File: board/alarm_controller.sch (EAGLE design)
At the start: 150 parts, among them IC3 AT24C, X1 RJ45-8L21-S, X2 RJ45-8L21-S

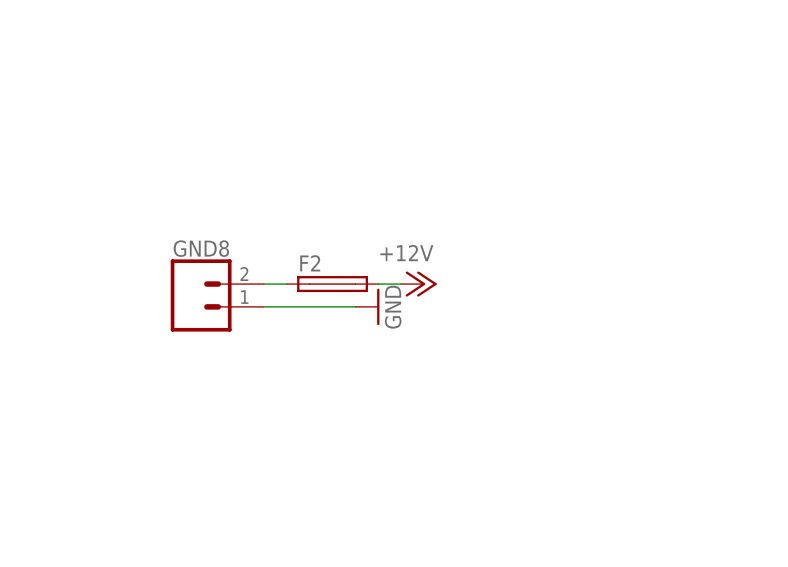
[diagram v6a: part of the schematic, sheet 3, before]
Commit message: swap pwr input for correct orientation
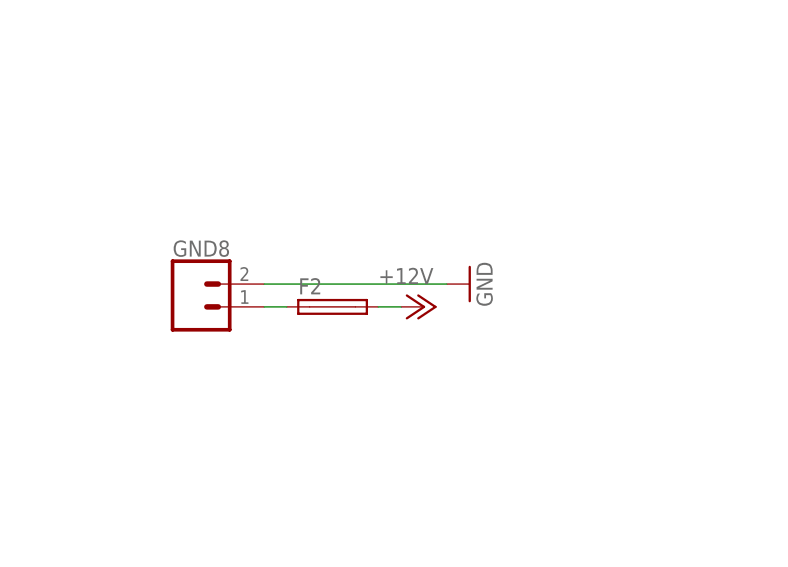
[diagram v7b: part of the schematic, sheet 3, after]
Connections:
- net GND: now also GND8.2; no longer GND8.1
- net PRE_FUSE_12V: now also GND8.1; no longer GND8.2
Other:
- moved on the sheet: F2
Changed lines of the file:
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@@
 <grid distance="0.1" unitdist="inch" unit="inch" style="lines" multiple="1" display="no" altdistance="0.01" altunitdist="inch" altunit="inch"/>
 <layers>
-<layer number="1" name="Top" color="4" fill="1" visible="yes" active="no"/>
-<layer number="2" name="Route2" color="1" fill="3" visible="yes" active="no"/>
-<layer number="3" name="Route3" color="4" fill="3" visible="yes" active="no"/>
-<layer number="4" name="Route4" color="1" fill="4" visible="yes" active="no"/>
-<layer number="5" name="Route5" color="4" fill="4" visible="yes" active="no"/>
-<layer number="6" name="Route6" color="1" fill="8" visible="yes" active="no"/>
-<layer number="7" name="Route7" color="4" fill="8" visible="yes" active="no"/>
-<layer number="8" name="Route8" color="1" fill="2" visible="yes" active="no"/>
-<layer number="9" name="Route9" color="4" fill="2" visible="yes" active="no"/>
-<layer number="10" name="Route10" color="1" fill="7" visible="yes" active="no"/>
-<layer number="11" name="Route11" color="4" fill="7" visible="yes" active="no"/>
-<layer number="12" name="Route12" color="1" fill="5" visible="yes" active="no"/>
-<layer number="13" name="Route13" color="4" fill="5" visible="yes" active="no"/>
-<layer number="14" name="Route14" color="1" fill="6" visible="yes" active="no"/>
-<layer number="15" name="Route15" color="4" fill="6" visible="yes" active="no"/>
-<layer number="16" name="Bottom" color="1" fill="1" visible="yes" active="no"/>
-<layer number="17" name="Pads" color="2" fill="1" visible="yes" active="no"/>
-<layer number="18" name="Vias" color="2" fill="1" visible="yes" active="no"/>
-<layer number="19" name="Unrouted" color="6" fill="1" visible="yes" active="no"/>
-<layer number="20" name="Dimension" color="15" fill="1" visible="yes" active="no"/>
-<layer number="21" name="tPlace" color="7" fill="1" visible="yes" active="no"/>
-<layer number="22" name="bPlace" color="7" fill="1" visible="yes" active="no"/>
-<layer number="23" name="tOrigins" color="15" fill="1" visible="yes" active="no"/>
-<layer number="24" name="bOrigins" color="15" fill="1" visible="yes" active="no"/>
-<layer number="25" name="tNames" color="7" fill="1" visible="yes" active="no"/>
-<layer number="26" name="bNames" color="7" fill="1" visible="yes" active="no"/>
-<layer number="27" name="tValues" color="7" fill="1" visible="yes" active="no"/>
-<layer number="28" name="bValues" color="7" fill="1" visible="yes" active="no"/>
+<layer number="1" name="Top" color="4" fill="1" visible="no" active="no"/>
+<layer number="2" name="Route2" color="1" fill="3" visible="no" active="no"/>
+<layer number="3" name="Route3" color="4" fill="3" visible="no" active="no"/>
+<layer number="4" name="Route4" color="1" fill="4" visible="no" active="no"/>
+<layer number="5" name="Route5" color="4" fill="4" visible="no" active="no"/>
+<layer number="6" name="Route6" color="1" fill="8" visible="no" active="no"/>
+<layer number="7" name="Route7" color="4" fill="8" visible="no" active="no"/>
+<layer number="8" name="Route8" color="1" fill="2" visible="no" active="no"/>
+<layer number="9" name="Route9" color="4" fill="2" visible="no" active="no"/>
+<layer number="10" name="Route10" color="1" fill="7" visible="no" active="no"/>
+<layer number="11" name="Route11" color="4" fill="7" visible="no" active="no"/>
+<layer number="12" name="Route12" color="1" fill="5" visible="no" active="no"/>
+<layer number="13" name="Route13" color="4" fill="5" visible="no" active="no"/>
+<layer number="14" name="Route14" color="1" fill="6" visible="no" active="no"/>
+<layer number="15" name="Route15" color="4" fill="6" visible="no" active="no"/>
+<layer number="16" name="Bottom" color="1" fill="1" visible="no" active="no"/>
+<layer number="17" name="Pads" color="2" fill="1" visible="no" active="no"/>
+<layer number="18" name="Vias" color="2" fill="1" visible="no" active="no"/>
+<layer number="19" name="Unrouted" color="6" fill="1" visible="no" active="no"/>
+<layer number="20" name="Dimension" color="15" fill="1" visible="no" active="no"/>
+<layer number="21" name="tPlace" color="7" fill="1" visible="no" active="no"/>
+<layer number="22" name="bPlace" color="7" fill="1" visible="no" active="no"/>
+<layer number="23" name="tOrigins" color="15" fill="1" visible="no" active="no"/>
+<layer number="24" name="bOrigins" color="15" fill="1" visible="no" active="no"/>
+<layer number="25" name="tNames" color="7" fill="1" visible="no" active="no"/>
+<layer number="26" name="bNames" color="7" fill="1" visible="no" active="no"/>
+<layer number="27" name="tValues" color="7" fill="1" visible="no" active="no"/>
+<layer number="28" name="bValues" color="7" fill="1" visible="no" active="no"/>
 <layer number="29" name="tStop" color="7" fill="3" visible="no" active="no"/>
 <layer number="30" name="bStop" color="7" fill="6" visible="no" active="no"/>
@@
 <layer number="35" name="tGlue" color="7" fill="4" visible="no" active="no"/>
 <layer number="36" name="bGlue" color="7" fill="5" visible="no" active="no"/>
-<layer number="37" name="tTest" color="7" fill="1" visible="yes" active="no"/>
-<layer number="38" name="bTest" color="7" fill="1" visible="yes" active="no"/>
+<layer number="37" name="tTest" color="7" fill="1" visible="no" active="no"/>
+<layer number="38" name="bTest" color="7" fill="1" visible="no" active="no"/>
 <layer number="39" name="tKeepout" color="4" fill="11" visible="no" active="no"/>
 <layer number="40" name="bKeepout" color="1" fill="11" visible="no" active="no"/>
@@
 <layer number="44" name="Drills" color="7" fill="1" visible="no" active="no"/>
 <layer number="45" name="Holes" color="7" fill="1" visible="no" active="no"/>
-<layer number="46" name="Milling" color="3" fill="1" visible="yes" active="no"/>
-<layer number="47" name="Measures" color="7" fill="1" visible="yes" active="no"/>
-<layer number="48" name="Document" color="7" fill="1" visible="yes" active="no"/>
-<layer number="49" name="Reference" color="7" fill="1" visible="yes" active="no"/>
-<layer number="50" name="dxf" color="7" fill="1" visible="yes" active="no"/>
-<layer number="51" name="tDocu" color="7" fill="1" visible="yes" active="no"/>
-<layer number="52" name="bDocu" color="7" fill="1" visible="yes" active="no"/>
-<layer number="53" name="tGND_GNDA" color="7" fill="9" visible="yes" active="no"/>
-<layer number="54" name="bGND_GNDA" color="1" fill="9" visible="yes" active="no"/>
-<layer number="56" name="wert" color="7" fill="1" visible="yes" active="no"/>
-<layer number="57" name="tCAD" color="7" fill="1" visible="yes" active="no"/>
-<layer number="59" name="tCarbon" color="7" fill="1" visible="yes" active="no"/>
-<layer number="60" name="bCarbon" color="7" fill="1" visible="yes" active="no"/>
+<layer number="46" name="Milling" color="3" fill="1" visible="no" active="no"/>
+<layer number="47" name="Measures" color="7" fill="1" visible="no" active="no"/>
+<layer number="48" name="Document" color="7" fill="1" visible="no" active="no"/>
+<layer number="49" name="Reference" color="7" fill="1" visible="no" active="no"/>
+<layer number="50" name="dxf" color="7" fill="1" visible="no" active="no"/>
+<layer number="51" name="tDocu" color="7" fill="1" visible="no" active="no"/>
+<layer number="52" name="bDocu" color="7" fill="1" visible="no" active="no"/>
+<layer number="53" name="tGND_GNDA" color="7" fill="9" visible="no" active="no"/>
+<layer number="54" name="bGND_GNDA" color="1" fill="9" visible="no" active="no"/>
+<layer number="56" name="wert" color="7" fill="1" visible="no" active="no"/>
+<layer number="57" name="tCAD" color="7" fill="1" visible="no" active="no"/>
+<layer number="59" name="tCarbon" color="7" fill="1" visible="no" active="no"/>
+<layer number="60" name="bCarbon" color="7" fill="1" visible="no" active="no"/>
 <layer number="90" name="Modules" color="5" fill="1" visible="yes" active="yes"/>
 <layer number="91" name="Nets" color="2" fill="1" visible="yes" active="yes"/>
@@
 <instance part="R62" gate="G$1" x="-81.28" y="35.56" rot="R180"/>
 <instance part="GND8" gate="G$1" x="-127" y="99.06"/>
-<instance part="F2" gate="1" x="-111.76" y="101.6"/>
-<instance part="P+8" gate="1" x="-101.6" y="101.6" rot="R270"/>
-<instance part="GND89" gate="1" x="-106.68" y="99.06" rot="R90"/>
+<instance part="F2" gate="1" x="-111.76" y="99.06"/>
+<instance part="P+8" gate="1" x="-101.6" y="99.06" rot="R270"/>
+<instance part="GND89" gate="1" x="-96.52" y="101.6" rot="R90"/>
 <instance part="12V2" gate="G$1" x="-43.18" y="35.56" rot="R180"/>
 <instance part="ALARMS3" gate="J$1" x="99.06" y="111.76"/>
@@
 </segment>
 <segment>
-<pinref part="GND8" gate="G$1" pin="1"/>
+<pinref part="GND8" gate="G$1" pin="2"/>
 <pinref part="GND89" gate="1" pin="GND"/>
-<wire x1="-119.38" y1="99.06" x2="-109.22" y2="99.06" width="0.1524" layer="91"/>
+<wire x1="-119.38" y1="101.6" x2="-99.06" y2="101.6" width="0.1524" layer="91"/>
 </segment>
 <segment>
@@
 <pinref part="F2" gate="1" pin="2"/>
 <pinref part="P+8" gate="1" pin="+12V"/>
-<wire x1="-106.68" y1="101.6" x2="-104.14" y2="101.6" width="0.1524" layer="91"/>
+<wire x1="-106.68" y1="99.06" x2="-104.14" y2="99.06" width="0.1524" layer="91"/>
 </segment>
 <segment>
@@
 <net name="PRE_FUSE_12V" class="0">
 <segment>
-<pinref part="GND8" gate="G$1" pin="2"/>
+<pinref part="GND8" gate="G$1" pin="1"/>
 <pinref part="F2" gate="1" pin="1"/>
-<wire x1="-119.38" y1="101.6" x2="-116.84" y2="101.6" width="0.1524" layer="91"/>
-</segment>
-</net>
+<wire x1="-119.38" y1="99.06" x2="-116.84" y2="99.06" width="0.1524" layer="91"/>
+</segment>
+</net>
